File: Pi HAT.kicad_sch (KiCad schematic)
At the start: 11 parts, among them J1 Screw_Terminal_01x04, J4 Barrel_Jack, J5 Screw_Terminal_01x03, J6 Screw_Terminal_01x03, J7 GPIO_CONNECTOR, Q1 S8550

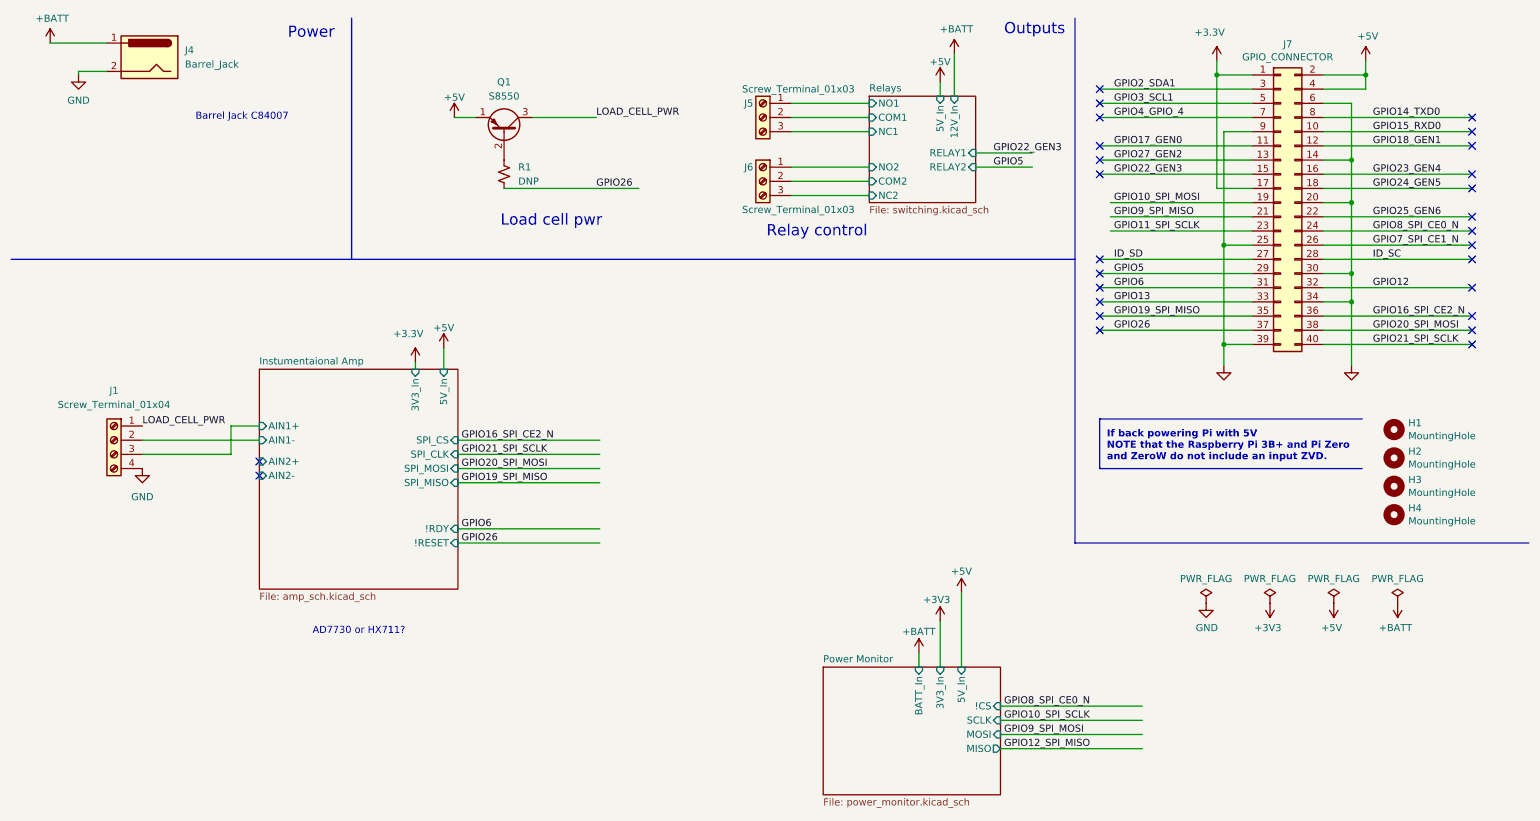
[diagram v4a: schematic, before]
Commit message: placement refinement and indicator LEDs for relays
-Crude wiring
-Fixed values
-Indicator LEDs for  relays
-Added test points
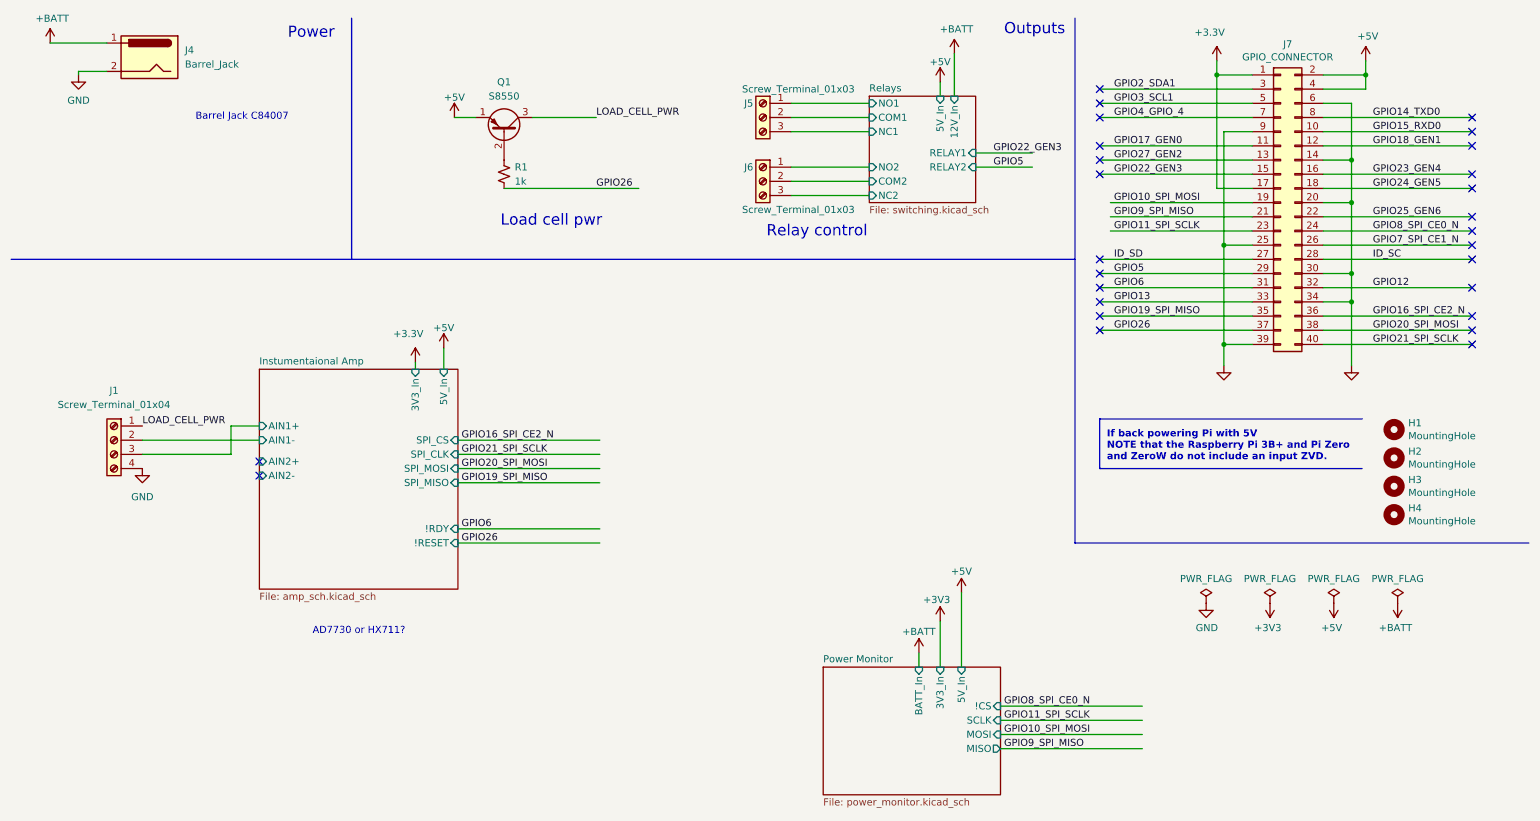
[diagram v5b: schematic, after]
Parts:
- R1: value DNP -> 1k
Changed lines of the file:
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@@
     (effects (font (size 1.27 1.27)) (justify left bottom))
   )
-  (label "GPIO10_SPI_SCLK" (at 190.5 138.43 0)
+  (label "GPIO11_SPI_SCLK" (at 190.5 138.43 0)
     (effects (font (size 1.27 1.27)) (justify left bottom))
   )
@@
     (effects (font (size 1.27 1.27)) (justify left bottom))
   )
-  (label "GPIO9_SPI_MOSI" (at 190.5 140.97 0)
+  (label "GPIO10_SPI_MOSI" (at 190.5 140.97 0)
     (effects (font (size 1.27 1.27)) (justify left bottom))
   )
@@
     (effects (font (size 1.27 1.27)) (justify left bottom))
   )
-  (label "GPIO12_SPI_MISO" (at 190.5 143.51 0)
+  (label "GPIO9_SPI_MISO" (at 190.5 143.51 0)
     (effects (font (size 1.27 1.27)) (justify left bottom))
   )
@@
   (symbol (lib_id "Device:R_Small_US") (at 100.965 40.64 0) (unit 1)
     (in_bom yes) (on_board yes) (fields_autoplaced)
-    (property "Reference" "R1" (id 0) (at 103.505 39.3699 0)
-      (effects (font (size 1.27 1.27)) (justify left))
-    )
-    (property "Value" "DNP" (id 1) (at 103.505 41.9099 0)
+    (property "Reference" "R1" (id 0) (at 102.87 39.3699 0)
+      (effects (font (size 1.27 1.27)) (justify left))
+    )
+    (property "Value" "1k" (id 1) (at 102.87 41.9099 0)
       (effects (font (size 1.27 1.27)) (justify left))
     )
@@
       (reference "D3") (unit 1) (value "LED_Small") (footprint "Diode_SMD:D_0603_1608Metric")
     )
+    (path "/d7c66af1-6c08-458e-8338-6725a48e4fd1/6f6108f7-6dad-4822-81d8-76cf1269693e"
+      (reference "D4") (unit 1) (value "LED_Small") (footprint "Diode_SMD:D_0603_1608Metric")
+    )
+    (path "/d7c66af1-6c08-458e-8338-6725a48e4fd1/3cf801d3-1c67-4a46-85de-edfa7a8697ed"
+      (reference "D5") (unit 1) (value "LED_Small") (footprint "Diode_SMD:D_0603_1608Metric")
+    )
     (path "/00000000-0000-0000-0000-00005c7c4c81"
       (reference "H1") (unit 1) (value "MountingHole") (footprint "lib:MountingHole_2.7mm_M2.5_uHAT_RPi")
@@
     )
     (path "/ecee919b-f163-4c81-8fec-579fb8377b40"
-      (reference "R1") (unit 1) (value "DNP") (footprint "Resistor_SMD:R_0402_1005Metric")
+      (reference "R1") (unit 1) (value "1k") (footprint "Resistor_SMD:R_0402_1005Metric")
     )
     (path "/5ec412a6-29a4-46a1-a19b-d00a58557335/9e78a024-04b9-4495-9b00-70110a769581"
-      (reference "R2") (unit 1) (value "4.7k") (footprint "Resistor_SMD:R_0402_1005Metric")
+      (reference "R2") (unit 1) (value "4k7") (footprint "Resistor_SMD:R_0402_1005Metric")
     )
     (path "/d7c66af1-6c08-458e-8338-6725a48e4fd1/f102247b-6560-48ca-b60c-63c1ceb549ee"
-      (reference "R3") (unit 1) (value "R_Small_US") (footprint "Resistor_SMD:R_0402_1005Metric")
+      (reference "R3") (unit 1) (value "1k") (footprint "Resistor_SMD:R_0402_1005Metric")
     )
     (path "/d7c66af1-6c08-458e-8338-6725a48e4fd1/937df843-9b15-43c3-a91b-9e0d26cab08f"
-      (reference "R4") (unit 1) (value "R_Small_US") (footprint "Resistor_SMD:R_0402_1005Metric")
+      (reference "R4") (unit 1) (value "1k") (footprint "Resistor_SMD:R_0402_1005Metric")
     )
     (path "/715798e8-ada1-4b31-bdfe-4378c151d2b8/00000000-0000-0000-0000-0000600e2945"
@@
     )
     (path "/715798e8-ada1-4b31-bdfe-4378c151d2b8/00000000-0000-0000-0000-00006018db0e"
-      (reference "R13") (unit 1) (value "DNP") (footprint "Resistor_SMD:R_0402_1005Metric")
+      (reference "R13") (unit 1) (value "220R") (footprint "Resistor_SMD:R_0402_1005Metric")
     )
     (path "/715798e8-ada1-4b31-bdfe-4378c151d2b8/00000000-0000-0000-0000-0000600df137"
@@
       (reference "R15") (unit 1) (value "33k") (footprint "Resistor_SMD:R_0402_1005Metric")
     )
+    (path "/d7c66af1-6c08-458e-8338-6725a48e4fd1/4907f08f-d94d-4477-a2c2-fc0c34bd299e"
+      (reference "R16") (unit 1) (value "1k") (footprint "Resistor_SMD:R_0402_1005Metric")
+    )
+    (path "/d7c66af1-6c08-458e-8338-6725a48e4fd1/7cd63105-13f9-4c3a-aabb-b92c656059ef"
+      (reference "R17") (unit 1) (value "1k") (footprint "Resistor_SMD:R_0402_1005Metric")
+    )
+    (path "/715798e8-ada1-4b31-bdfe-4378c151d2b8/cca3808a-d6bb-44a3-ad1d-2a1c034fb726"
+      (reference "TP1") (unit 1) (value "TestPoint") (footprint "TestPoint:TestPoint_Pad_D1.5mm")
+    )
+    (path "/715798e8-ada1-4b31-bdfe-4378c151d2b8/73e3223a-0afd-438b-8fcb-933535615d47"
+      (reference "TP2") (unit 1) (value "TestPoint") (footprint "TestPoint:TestPoint_Pad_D1.5mm")
+    )
+    (path "/715798e8-ada1-4b31-bdfe-4378c151d2b8/6caf196e-dcfe-4294-9da5-689e6f22f042"
+      (reference "TP3") (unit 1) (value "TestPoint") (footprint "TestPoint:TestPoint_Pad_D1.5mm")
+    )
+    (path "/715798e8-ada1-4b31-bdfe-4378c151d2b8/3b600e6a-acbe-4f8c-ad56-d17f4e961218"
+      (reference "TP4") (unit 1) (value "TestPoint") (footprint "TestPoint:TestPoint_Pad_D1.5mm")
+    )
+    (path "/5ec412a6-29a4-46a1-a19b-d00a58557335/e5da6f3f-d704-4afe-8d35-e0a9bac612ad"
+      (reference "TP5") (unit 1) (value "TestPoint") (footprint "TestPoint:TestPoint_Pad_D1.5mm")
+    )
+    (path "/5ec412a6-29a4-46a1-a19b-d00a58557335/930e7413-54b4-413f-893f-53f4d79f75d3"
+      (reference "TP6") (unit 1) (value "TestPoint") (footprint "TestPoint:TestPoint_Pad_D1.5mm")
+    )
+    (path "/5ec412a6-29a4-46a1-a19b-d00a58557335/d472f7d5-fbb6-4635-a88a-990bcb3df520"
+      (reference "TP7") (unit 1) (value "TestPoint") (footprint "TestPoint:TestPoint_Pad_D1.5mm")
+    )
+    (path "/5ec412a6-29a4-46a1-a19b-d00a58557335/15677da5-436a-4f43-9049-14daec4c3531"
+      (reference "TP8") (unit 1) (value "TestPoint") (footprint "TestPoint:TestPoint_Pad_D1.5mm")
+    )
     (path "/5ec412a6-29a4-46a1-a19b-d00a58557335/efbe0f43-2997-43b2-b307-a9e0d23db53f"

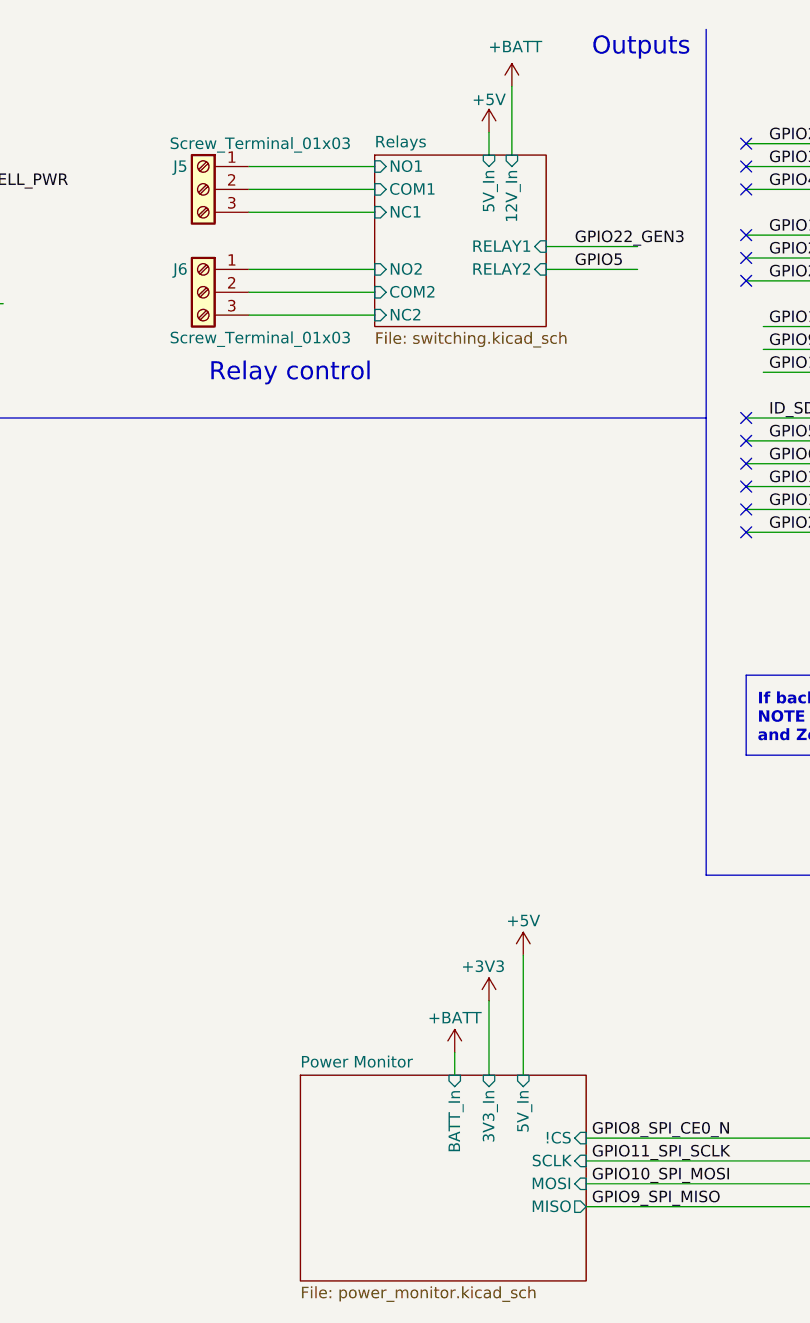
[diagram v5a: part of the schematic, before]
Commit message: Wiring and 12V battery_sensed added
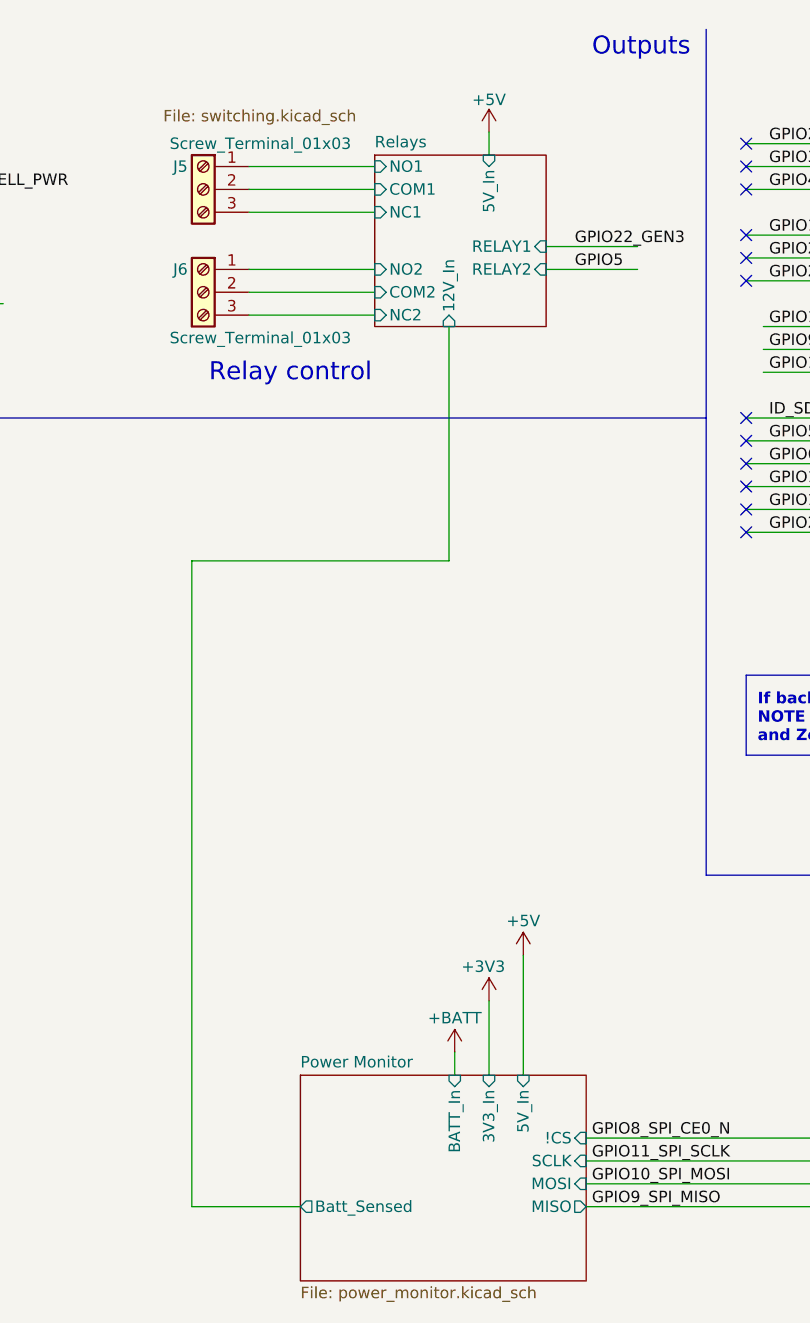
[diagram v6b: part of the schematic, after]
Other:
- sheet Power Monitor ports: added Batt_Sensed; removed none
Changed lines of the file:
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@@
+    (stroke (width 0) (type default) (color 0 0 0 0))
+  )
+  (wire (pts (xy 146.05 71.755) (xy 174.625 71.755))
     (stroke (width 0) (type default) (color 0 0 0 0))
   )
@@
     (stroke (width 0) (type default) (color 0 0 0 0))
   )
-  (wire (pts (xy 181.61 19.05) (xy 181.61 26.67))
-    (stroke (width 0) (type default) (color 0 0 0 0))
-  )
   (polyline (pts (xy 203.2 12.7) (xy 203.2 106.68))
     (stroke (width 0) (type default) (color 0 0 0 0))
@@
     (stroke (width 0) (type default) (color 0 0 0 0))
   )
+  (wire (pts (xy 158.115 143.51) (xy 146.05 143.51))
+    (stroke (width 0) (type default) (color 0 0 0 0))
+  )
   (wire (pts (xy 92.075 30.48) (xy 95.885 30.48))
     (stroke (width 0) (type default) (color 0 0 0 0))
@@
     (stroke (width 0) (type default) (color 0 0 0 0))
   )
+  (wire (pts (xy 146.05 143.51) (xy 146.05 71.755))
+    (stroke (width 0) (type default) (color 0 0 0 0))
+  )
   (wire (pts (xy 19.685 17.145) (xy 29.845 17.145))
+    (stroke (width 0) (type default) (color 0 0 0 0))
+  )
+  (wire (pts (xy 174.625 71.755) (xy 174.625 45.72))
     (stroke (width 0) (type default) (color 0 0 0 0))
   )
@@
     (pin "1")
   )
-  (symbol (lib_id "power:+BATT") (at 181.61 19.05 0) (unit 1)
-    (in_bom yes) (on_board yes)
-    (property "Reference" "#PWR015" (id 0) (at 181.61 22.86 0)
-      (effects (font (size 1.27 1.27)) hide)
-    )
-    (property "Value" "+BATT" (id 1) (at 181.991 14.6558 0))
-    (property "Footprint" "" (id 2) (at 181.61 19.05 0)
-      (effects (font (size 1.27 1.27)) hide)
-    )
-    (property "Datasheet" "" (id 3) (at 181.61 19.05 0)
-      (effects (font (size 1.27 1.27)) hide)
-    )
-    (pin "1")
-  )
   (symbol (lib_id "power:+3V3") (at 238.125 117.475 180) (unit 1)
     (in_bom yes) (on_board yes)
@@
       (effects (font (size 1.27 1.27)) (justify right))
     )
-  )
-  (sheet (at 166.37 26.67) (size 19.05 19.05) (fields_autoplaced)
+    (pin "Batt_Sensed" output (at 158.115 143.51 180)
+      (effects (font (size 1.27 1.27)) (justify left))
+    )
+  )
+  (sheet (at 166.37 26.67) (size 19.05 19.05)
     (stroke (width 0.1524) (type solid) (color 0 0 0 0))
     (fill (color 0 0 0 0.0000))
@@
       (effects (font (size 1.27 1.27)) (justify left bottom))
     )
-    (property "Sheet file" "switching.kicad_sch" (id 1) (at 166.37 46.3046 0)
+    (property "Sheet file" "switching.kicad_sch" (id 1) (at 142.875 21.59 0)
       (effects (font (size 1.27 1.27)) (justify left top))
     )
@@
       (effects (font (size 1.27 1.27)) (justify left))
     )
-    (pin "12V_In" input (at 181.61 26.67 90)
-      (effects (font (size 1.27 1.27)) (justify right))
+    (pin "12V_In" input (at 174.625 45.72 270)
+      (effects (font (size 1.27 1.27)) (justify left))
     )
   )
@@
       (reference "#PWR014") (unit 1) (value "+3V3") (footprint "")
     )
-    (path "/d093daa1-4942-4396-834a-be78a67a5288"
-      (reference "#PWR015") (unit 1) (value "+BATT") (footprint "")
-    )
     (path "/4bc749eb-7b65-443f-8136-78cf9e78c5e4"
       (reference "#PWR016") (unit 1) (value "+5V") (footprint "")
@@
       (reference "#PWR037") (unit 1) (value "GND") (footprint "")
     )
-    (path "/715798e8-ada1-4b31-bdfe-4378c151d2b8/00000000-0000-0000-0000-0000601b33ef"
-      (reference "#PWR038") (unit 1) (value "GND") (footprint "")
-    )
     (path "/715798e8-ada1-4b31-bdfe-4378c151d2b8/00000000-0000-0000-0000-0000601b3eb3"
       (reference "#PWR039") (unit 1) (value "+5V") (footprint "")
@@
       (reference "J7") (unit 1) (value "GPIO_CONNECTOR") (footprint "lib:PinSocket_2x20_P2.54mm_Vertical_Centered_Anchor")
     )
-    (path "/715798e8-ada1-4b31-bdfe-4378c151d2b8/00000000-0000-0000-0000-0000601b1ca2"
-      (reference "J8") (unit 1) (value "Conn_01x03_Male") (footprint "Connector_PinHeader_2.54mm:PinHeader_1x03_P2.54mm_Vertical")
-    )
     (path "/715798e8-ada1-4b31-bdfe-4378c151d2b8/00000000-0000-0000-0000-0000601af8e8"
       (reference "J9") (unit 1) (value "Conn_01x03_Male") (footprint "Connector_PinHeader_2.54mm:PinHeader_1x03_P2.54mm_Vertical")
     )
-    (path "/715798e8-ada1-4b31-bdfe-4378c151d2b8/00000000-0000-0000-0000-0000601d37e1"
-      (reference "J10") (unit 1) (value "Conn_01x03_Male") (footprint "Connector_PinHeader_2.54mm:PinHeader_1x03_P2.54mm_Vertical")
-    )
     (path "/715798e8-ada1-4b31-bdfe-4378c151d2b8/00000000-0000-0000-0000-000060149cd0"
       (reference "J11") (unit 1) (value "Conn_01x02_Male") (footprint "Connector_PinHeader_2.54mm:PinHeader_1x02_P2.54mm_Vertical")
@@
       (reference "JP6") (unit 1) (value "Jumper_NO_Small") (footprint "Jumper:SolderJumper-2_P1.3mm_Open_RoundedPad1.0x1.5mm")
     )
+    (path "/715798e8-ada1-4b31-bdfe-4378c151d2b8/5e0ee9bc-e95e-43cb-8bbe-4cc91e620905"
+      (reference "JP7") (unit 1) (value "Jumper_3_Open") (footprint "Jumper:SolderJumper-3_P2.0mm_Open_TrianglePad1.0x1.5mm")
+    )
     (path "/d7c66af1-6c08-458e-8338-6725a48e4fd1/d7324371-8ba6-4f3e-a6c7-87b894d947b9"
